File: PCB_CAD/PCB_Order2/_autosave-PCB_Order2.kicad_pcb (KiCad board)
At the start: 4 copper layers, 105.5 x 59.5 mm, 58 parts

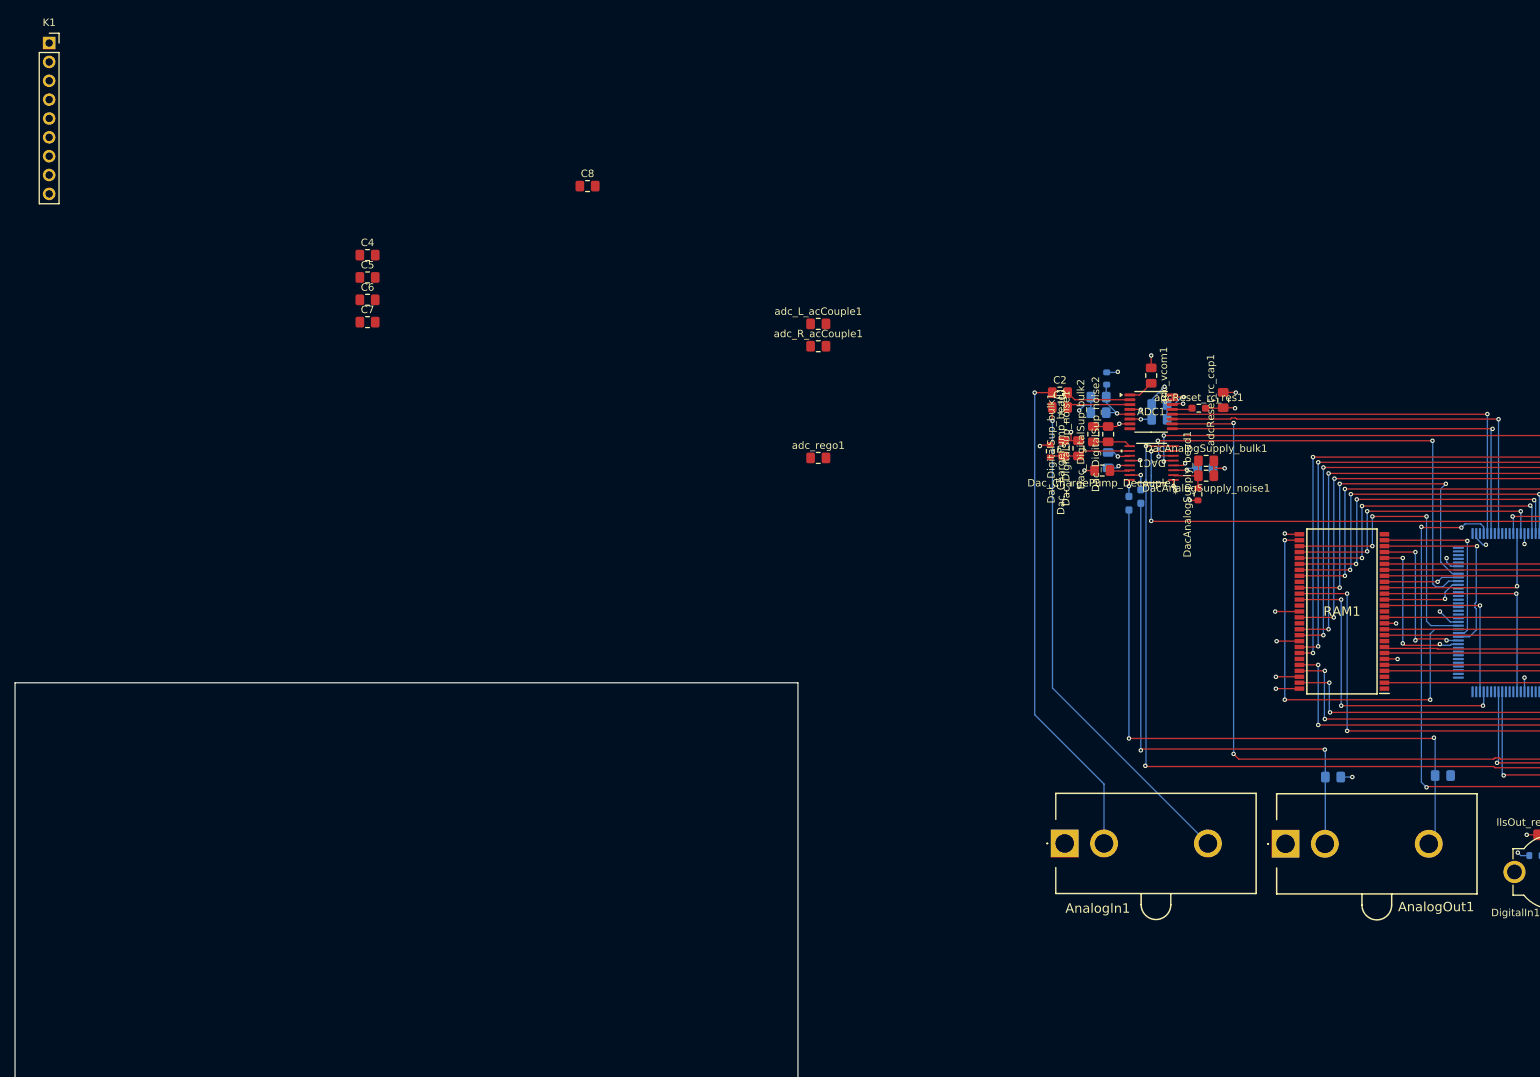
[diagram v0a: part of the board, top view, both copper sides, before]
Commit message: added footprints
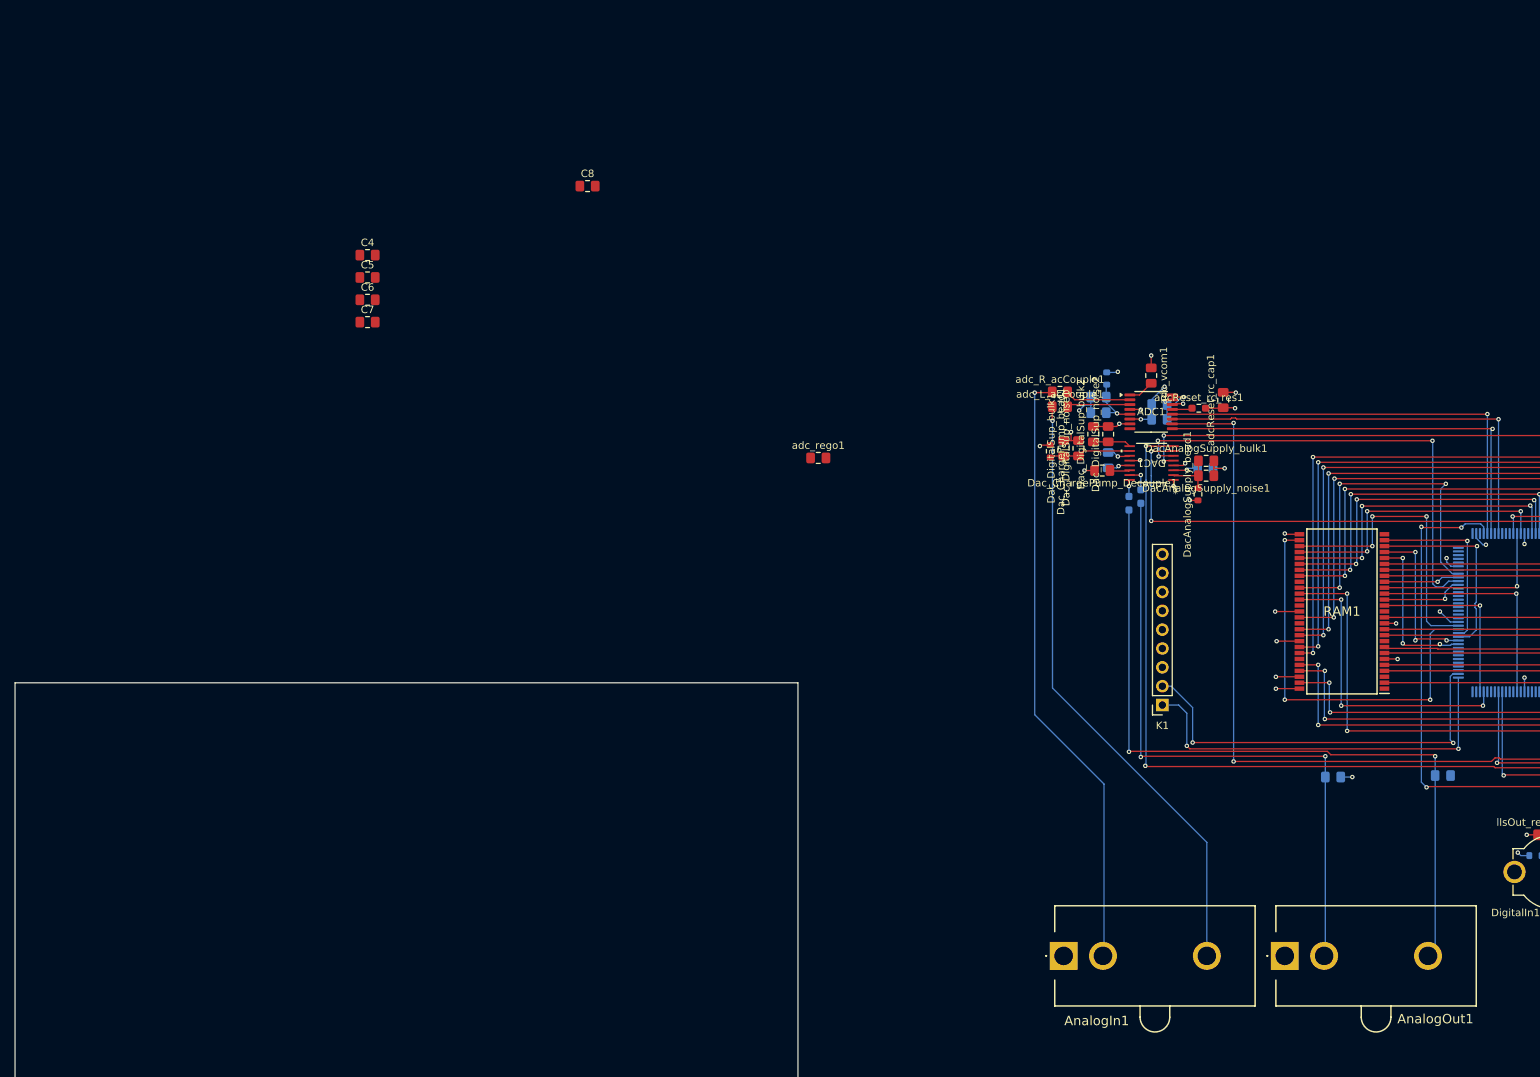
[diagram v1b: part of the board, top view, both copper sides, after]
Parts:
- removed C2, C3: 10uF, Capacitor_SMD:C_0805_2012Metric_Pad1.18x1.45mm_HandSolder
- moved K1 174.5 mm to (175.0, 135.8), turned to 180 degrees
- moved adc_L_acCouple1 34.4 mm to (161.2, 95.6)
- moved adc_R_acCouple1 33.1 mm to (161.2, 93.6)
- moved AnalogIn1 15.2 mm to (161.7, 169.6)
- moved AnalogOut1 15.1 mm to (191.5, 169.6)
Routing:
- net /KP_Col4: track 0.00 -> 55.5 mm, vias 0 -> 2
- net /KP_Col5: track 0.00 -> 54.5 mm, vias 0 -> 2
- net Net-(AnalogIn1-Pad2): track 67.0 -> 82.2 mm
- net Net-(AnalogOut1-Pad2): track 70.9 -> 86.1 mm
- net Net-(AnalogIn1-Pad3): track 67.4 -> 82.5 mm
- net Net-(AnalogOut1-Pad3): track 86.7 -> 101.4 mm
- net /I2S1_WS: track 112.8 -> 113.7 mm
